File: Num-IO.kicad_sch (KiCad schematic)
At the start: 8 parts, among them U3 MAX14851AEE+

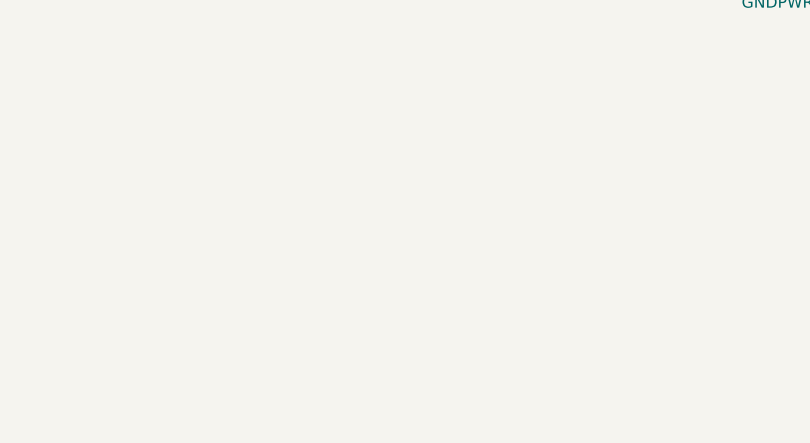
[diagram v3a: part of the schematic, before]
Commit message: Basic routing done, cheating a bit on the diff + add holes (to be positionned)
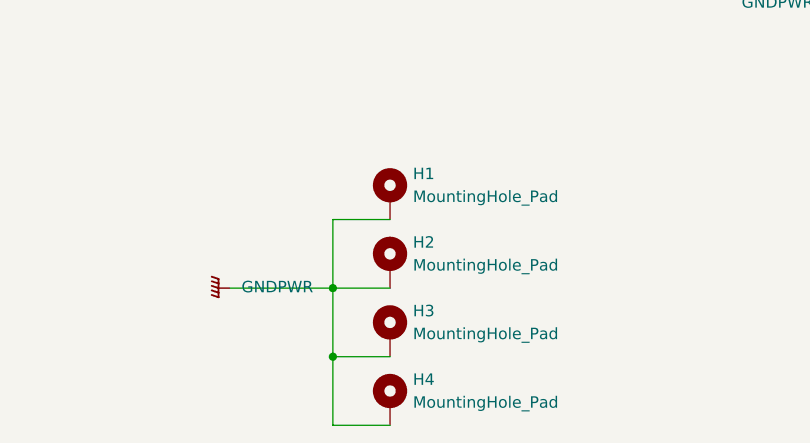
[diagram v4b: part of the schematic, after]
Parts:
- added H1, H2, H3, H4: MountingHole_Pad, MountingHole:MountingHole_3.2mm_M3_DIN965_Pad, symbol Mechanical:MountingHole_Pad
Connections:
- net GNDPWR: now also H1.1, H2.1, H3.1, H4.1
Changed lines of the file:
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@@
   (junction (at 72.39 63.5) (diameter 0) (color 0 0 0 0)
   )
+  (junction (at 68.58 177.8) (diameter 0) (color 0 0 0 0)
+  )
   (junction (at 73.66 96.52) (diameter 0) (color 0 0 0 0)
   )
@@
   )
   (junction (at 73.66 66.04) (diameter 0) (color 0 0 0 0)
+  )
+  (junction (at 68.58 185.42) (diameter 0) (color 0 0 0 0)
   )
   (junction (at 212.09 74.93) (diameter 0) (color 0 0 0 0)
@@
     (stroke (width 0) (type default) (color 0 0 0 0))
   )
+  (wire (pts (xy 68.58 185.42) (xy 68.58 177.8))
+    (stroke (width 0) (type default) (color 0 0 0 0))
+  )
   (wire (pts (xy 43.18 106.68) (xy 45.72 106.68))
     (stroke (width 0) (type default) (color 0 0 0 0))
@@
     (stroke (width 0) (type default) (color 0 0 0 0))
   )
+  (wire (pts (xy 68.58 193.04) (xy 74.93 193.04))
+    (stroke (width 0) (type default) (color 0 0 0 0))
+  )
   (wire (pts (xy 43.18 38.1) (xy 45.72 38.1))
     (stroke (width 0) (type default) (color 0 0 0 0))
@@
     (stroke (width 0) (type default) (color 0 0 0 0))
   )
+  (wire (pts (xy 57.15 177.8) (xy 68.58 177.8))
+    (stroke (width 0) (type default) (color 0 0 0 0))
+  )
+  (wire (pts (xy 68.58 185.42) (xy 68.58 193.04))
+    (stroke (width 0) (type default) (color 0 0 0 0))
+  )
   (wire (pts (xy 72.39 93.98) (xy 72.39 123.19))
     (stroke (width 0) (type default) (color 0 0 0 0))
@@
     (stroke (width 0) (type default) (color 0 0 0 0))
   )
+  (wire (pts (xy 74.93 170.18) (xy 68.58 170.18))
+    (stroke (width 0) (type default) (color 0 0 0 0))
+  )
+  (wire (pts (xy 74.93 185.42) (xy 68.58 185.42))
+    (stroke (width 0) (type default) (color 0 0 0 0))
+  )
   (wire (pts (xy 252.73 125.73) (xy 255.27 125.73))
     (stroke (width 0) (type default) (color 0 0 0 0))
@@
     (stroke (width 0) (type default) (color 0 0 0 0))
   )
+  (wire (pts (xy 68.58 177.8) (xy 74.93 177.8))
+    (stroke (width 0) (type default) (color 0 0 0 0))
+  )
   (wire (pts (xy 66.04 120.65) (xy 71.12 120.65))
     (stroke (width 0) (type default) (color 0 0 0 0))
@@
   )
   (wire (pts (xy 214.63 69.85) (xy 224.79 69.85))
+    (stroke (width 0) (type default) (color 0 0 0 0))
+  )
+  (wire (pts (xy 68.58 170.18) (xy 68.58 177.8))
     (stroke (width 0) (type default) (color 0 0 0 0))
   )
@@
     (pin "1")
   )
+  (symbol (lib_id "Mechanical:MountingHole_Pad") (at 74.93 190.5 0) (unit 1)
+    (in_bom yes) (on_board yes) (fields_autoplaced)
+    (property "Reference" "H4" (id 0) (at 77.47 187.9599 0)
+      (effects (font (size 1.27 1.27)) (justify left))
+    )
+    (property "Value" "MountingHole_Pad" (id 1) (at 77.47 190.4999 0)
+      (effects (font (size 1.27 1.27)) (justify left))
+    )
+    (property "Footprint" "MountingHole:MountingHole_3.2mm_M3_DIN965_Pad" (id 2) (at 74.93 190.5 0)
+      (effects (font (size 1.27 1.27)) hide)
+    )
+    (property "Datasheet" "~" (id 3) (at 74.93 190.5 0)
+      (effects (font (size 1.27 1.27)) hide)
+    )
+    (pin "1")
+  )
+  (symbol (lib_id "Mechanical:MountingHole_Pad") (at 74.93 182.88 0) (unit 1)
+    (in_bom yes) (on_board yes) (fields_autoplaced)
+    (property "Reference" "H3" (id 0) (at 77.47 180.3399 0)
+      (effects (font (size 1.27 1.27)) (justify left))
+    )
+    (property "Value" "MountingHole_Pad" (id 1) (at 77.47 182.8799 0)
+      (effects (font (size 1.27 1.27)) (justify left))
+    )
+    (property "Footprint" "MountingHole:MountingHole_3.2mm_M3_DIN965_Pad" (id 2) (at 74.93 182.88 0)
+      (effects (font (size 1.27 1.27)) hide)
+    )
+    (property "Datasheet" "~" (id 3) (at 74.93 182.88 0)
+      (effects (font (size 1.27 1.27)) hide)
+    )
+    (pin "1")
+  )
+  (symbol (lib_id "Mechanical:MountingHole_Pad") (at 74.93 167.64 0) (unit 1)
+    (in_bom yes) (on_board yes) (fields_autoplaced)
+    (property "Reference" "H1" (id 0) (at 77.47 165.0999 0)
+      (effects (font (size 1.27 1.27)) (justify left))
+    )
+    (property "Value" "MountingHole_Pad" (id 1) (at 77.47 167.6399 0)
+      (effects (font (size 1.27 1.27)) (justify left))
+    )
+    (property "Footprint" "MountingHole:MountingHole_3.2mm_M3_DIN965_Pad" (id 2) (at 74.93 167.64 0)
+      (effects (font (size 1.27 1.27)) hide)
+    )
+    (property "Datasheet" "~" (id 3) (at 74.93 167.64 0)
+      (effects (font (size 1.27 1.27)) hide)
+    )
+    (pin "1")
+  )
   (symbol (lib_id "Device:R") (at 161.29 88.9 0) (unit 1)
     (in_bom yes) (on_board yes) (fields_autoplaced)
@@
     (pin "1")
     (pin "2")
+  )
+  (symbol (lib_id "Mechanical:MountingHole_Pad") (at 74.93 175.26 0) (unit 1)
+    (in_bom yes) (on_board yes) (fields_autoplaced)
+    (property "Reference" "H2" (id 0) (at 77.47 172.7199 0)
+      (effects (font (size 1.27 1.27)) (justify left))
+    )
+    (property "Value" "MountingHole_Pad" (id 1) (at 77.47 175.2599 0)
+      (effects (font (size 1.27 1.27)) (justify left))
+    )
+    (property "Footprint" "MountingHole:MountingHole_3.2mm_M3_DIN965_Pad" (id 2) (at 74.93 175.26 0)
+      (effects (font (size 1.27 1.27)) hide)
+    )
+    (property "Datasheet" "~" (id 3) (at 74.93 175.26 0)
+      (effects (font (size 1.27 1.27)) hide)
+    )
+    (pin "1")
   )
   (symbol (lib_id "Device:C") (at 127 57.15 90) (unit 1)
@@
     )
     (property "Datasheet" "" (id 3) (at 148.59 58.42 0)
+      (effects (font (size 1.27 1.27)) hide)
+    )
+    (pin "1")
+  )
+  (symbol (lib_id "power:GNDPWR") (at 57.15 177.8 270) (unit 1)
+    (in_bom yes) (on_board yes) (fields_autoplaced)
+    (property "Reference" "#PWR094" (id 0) (at 52.07 177.8 0)
+      (effects (font (size 1.27 1.27)) hide)
+    )
+    (property "Value" "GNDPWR" (id 1) (at 58.42 177.6729 90)
+      (effects (font (size 1.27 1.27)) (justify left))
+    )
+    (property "Footprint" "" (id 2) (at 55.88 177.8 0)
+      (effects (font (size 1.27 1.27)) hide)
+    )
+    (property "Datasheet" "" (id 3) (at 55.88 177.8 0)
       (effects (font (size 1.27 1.27)) hide)
     )
@@
       (reference "#PWR093") (unit 1) (value "GNDD") (footprint "")
     )
+    (path "/e8c96f1c-0c26-4518-b37c-f08cf479c5c9"
+      (reference "#PWR094") (unit 1) (value "GNDPWR") (footprint "")
+    )
     (path "/94eb0688-f710-4c77-a991-98d54924db98/12393bb7-cbb7-41d4-afd0-c2062de5fe4c"
       (reference "C1") (unit 1) (value "1uF") (footprint "Capacitor_SMD:C_1210_3225Metric")
@@
       (reference "D2") (unit 1) (value "1N4007") (footprint "Diode_SMD:D_MELF")
     )
+    (path "/6ab8bceb-495f-4cab-b0d4-04698939a995"
+      (reference "H1") (unit 1) (value "MountingHole_Pad") (footprint "MountingHole:MountingHole_3.2mm_M3_DIN965_Pad")
+    )
+    (path "/7eecdbcc-749c-49d1-8a81-195f60462cf1"
+      (reference "H2") (unit 1) (value "MountingHole_Pad") (footprint "MountingHole:MountingHole_3.2mm_M3_DIN965_Pad")
+    )
+    (path "/671730bd-8cc6-48be-87f1-a6d63b54921b"
+      (reference "H3") (unit 1) (value "MountingHole_Pad") (footprint "MountingHole:MountingHole_3.2mm_M3_DIN965_Pad")
+    )
+    (path "/61bfba10-0676-4210-8752-7ac3fd2a77e6"
+      (reference "H4") (unit 1) (value "MountingHole_Pad") (footprint "MountingHole:MountingHole_3.2mm_M3_DIN965_Pad")
+    )
     (path "/f406686c-9281-4d3d-803f-df6f4de4bd3f/eb79cea9-fa97-475b-90d4-17b2843503f4"
       (reference "J1") (unit 1) (value "DB37_Female") (footprint "Connector_Dsub:DSUB-37_Female_Horizontal_P2.77x2.54mm_EdgePinOffset9.40mm")
@@
     )
     (path "/1d55f859-b955-4956-adf8-4e32f584531b/e1320af5-6f7d-4e2d-89e2-43ceb3beb950"
-      (reference "U9") (unit 1) (value "LTC6820IUD") (footprint "Maxim industrial IO:LTC6820IUD")
+      (reference "U9") (unit 1) (value "LTC6820IUD") (footprint "QFN-16_UD_AA_ADI")
     )
     (path "/1d55f859-b955-4956-adf8-4e32f584531b/a7412f16-2cbc-499f-b1a6-0f7a73b82712"
-      (reference "U10") (unit 1) (value "LTC6820IUD") (footprint "Maxim industrial IO:LTC6820IUD")
+      (reference "U10") (unit 1) (value "LTC6820IUD") (footprint "QFN-16_UD_AA_ADI")
     )
     (path "/1d55f859-b955-4956-adf8-4e32f584531b/79d4eaed-588f-49d0-b052-d174c0038e0a"
-      (reference "U11") (unit 1) (value "LTC6820IUD") (footprint "Maxim industrial IO:LTC6820IUD")
+      (reference "U11") (unit 1) (value "LTC6820IUD") (footprint "QFN-16_UD_AA_ADI")
     )
     (path "/1d55f859-b955-4956-adf8-4e32f584531b/4b95657c-1f29-4217-8703-ec40500ff92c"
-      (reference "U12") (unit 1) (value "LTC6820IUD") (footprint "Maxim industrial IO:LTC6820IUD")
-    )
-  )
+      (reference "U12") (unit 1) (value "LTC6820IUD") (footprint "QFN-16_UD_AA_ADI")
+    )
+  )

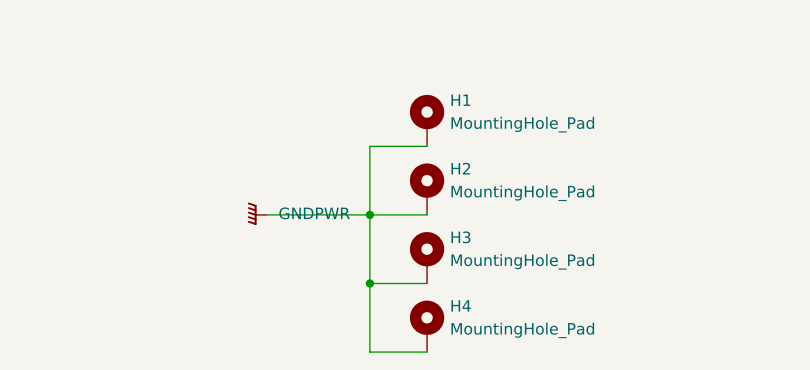
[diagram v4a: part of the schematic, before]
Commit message: change package QFN => MSOP
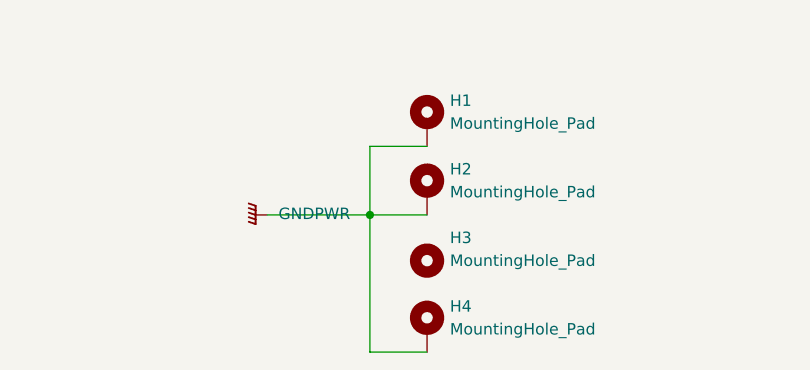
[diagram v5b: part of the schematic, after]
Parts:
- H3: symbol Mechanical:MountingHole_Pad -> Mechanical:MountingHole
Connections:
- net GNDPWR: no longer H3.1

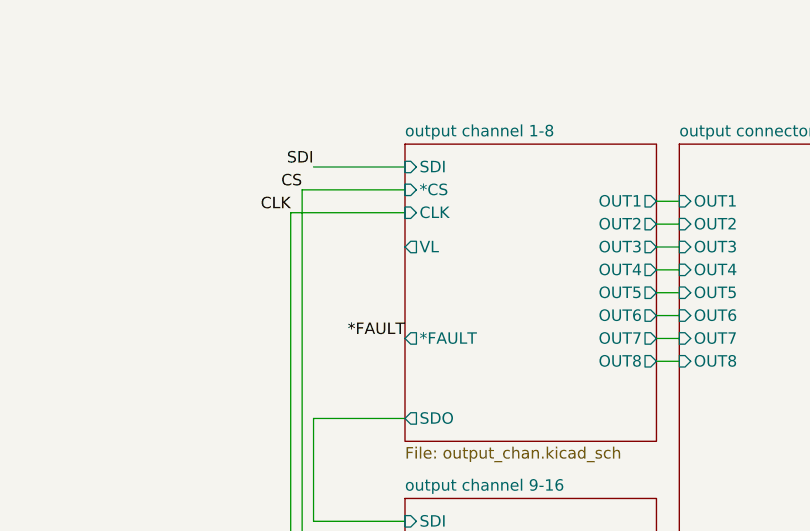
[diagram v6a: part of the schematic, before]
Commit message: fix a few warnings
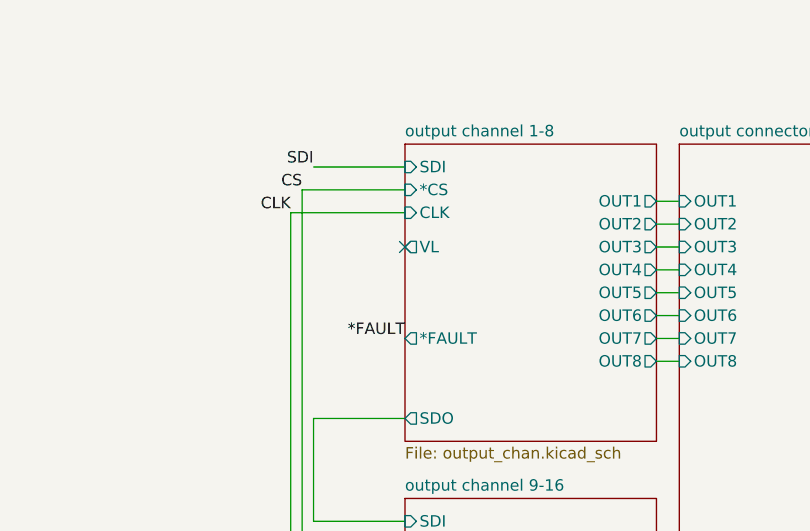
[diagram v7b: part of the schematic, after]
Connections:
- no-connect marks 7 -> 8

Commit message: fix most errors/warnings
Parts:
- added R28, R29: 100k, Resistor_SMD:R_0603_1608Metric, symbol Device:R
- added R30: 3.3k, Resistor_SMD:R_0603_1608Metric, symbol Device:R
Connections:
- net GNDD: now also R29.2
- net GNDPWR: now also R28.1, R30.2
- net at U3.10 (I/OB2): now also R30.1
- net at U3.7 (I/OA2): now also R29.1
- new net output channel 17-24/SDO: R28.2
